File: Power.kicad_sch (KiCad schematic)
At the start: 34 parts, among them U1 LP87702DRHBRQ1

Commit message: finding exact crystal used in ref design, finishing shcematics
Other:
- note added: "Decoupling Caps"
- note added: "LC filtering"
- note added: "volt regulators, battery charger, and stepdowns"
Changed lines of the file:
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@@
+    (effects (font (size 1.27 1.27)) (justify left bottom))
+  )
+  (text "LC filtering\n" (at 243.84 66.04 0)
+    (effects (font (size 1.27 1.27)) (justify left bottom))
+  )
+  (text "volt regulators, battery charger, and stepdowns" (at 228.6 17.78 0)
+    (effects (font (size 1.27 1.27)) (justify left bottom))
+  )
+  (text "Decoupling Caps\n" (at 241.3 92.71 0)
     (effects (font (size 1.27 1.27)) (justify left bottom))
   )

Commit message: squashing ERC errors
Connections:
- net +3V3: no longer C1.2, C2.2, C3.1, C4.1, L1.2, R1.1, R2.1, R3.1, R4.1, U1.13 (VIN_B1), U1.14 (VIN_B1), U1.27 (VIN_B0), U1.28 (VIN_B0)
- net 1V24: no longer R8.2
- net 1V8: no longer R9.2
- net PMIC_EN1 renamed 3V3_REF
- net 3V3_REF: now also C1.2, C2.2, C3.1, C4.1, L1.2, R1.1, R2.1, R3.1, R4.1, U1.13 (VIN_B1), U1.14 (VIN_B1), U1.27 (VIN_B0), U1.28 (VIN_B0)
- new net AWR_1V24: R8.2
- new net AWR_1V8: R9.2
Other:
- note added: "voltage monitoring 1V24"
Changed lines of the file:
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@@
   (junction (at 60.96 166.37) (diameter 0) (color 0 0 0 0)
+  )
+  (junction (at 25.4 115.57) (diameter 0) (color 0 0 0 0)
   )
   (junction (at 146.05 162.56) (diameter 0) (color 0 0 0 0)
@@
     (stroke (width 0) (type default))
   )
-  (wire (pts (xy 45.72 113.03) (xy 41.91 113.03))
+  (wire (pts (xy 25.4 111.76) (xy 53.34 111.76))
     (stroke (width 0) (type default))
   )
@@
     (stroke (width 0) (type default))
   )
+  (wire (pts (xy 25.4 115.57) (xy 25.4 121.92))
+    (stroke (width 0) (type default))
+  )
   (wire (pts (xy 179.07 86.36) (xy 179.07 90.17))
     (stroke (width 0) (type default))
@@
     (stroke (width 0) (type default))
   )
-  (wire (pts (xy 52.07 104.14) (xy 52.07 110.49))
+  (wire (pts (xy 53.34 104.14) (xy 53.34 111.76))
     (stroke (width 0) (type default))
   )
@@
     (stroke (width 0) (type default))
   )
-  (wire (pts (xy 36.83 121.92) (xy 24.13 121.92))
+  (wire (pts (xy 36.83 121.92) (xy 25.4 121.92))
     (stroke (width 0) (type default))
   )
@@
     (stroke (width 0) (type default))
   )
-  (wire (pts (xy 52.07 110.49) (xy 45.72 110.49))
-    (stroke (width 0) (type default))
-  )
   (wire (pts (xy 148.59 101.6) (xy 154.94 101.6))
     (stroke (width 0) (type default))
@@
     (stroke (width 0) (type default))
   )
-  (wire (pts (xy 45.72 110.49) (xy 45.72 113.03))
-    (stroke (width 0) (type default))
-  )
   (wire (pts (xy 76.2 116.84) (xy 76.2 128.27))
     (stroke (width 0) (type default))
@@
     (stroke (width 0) (type default))
   )
+  (wire (pts (xy 25.4 111.76) (xy 25.4 115.57))
+    (stroke (width 0) (type default))
+  )
   (wire (pts (xy 34.29 73.66) (xy 40.64 73.66))
     (stroke (width 0) (type default))
@@
     (stroke (width 0) (type default))
   )
+  (wire (pts (xy 22.86 115.57) (xy 25.4 115.57))
+    (stroke (width 0) (type default))
+  )
   (wire (pts (xy 68.58 111.76) (xy 68.58 157.48))
     (stroke (width 0) (type default))
@@
     (stroke (width 0) (type default))
   )
-  (wire (pts (xy 50.8 158.75) (xy 50.8 161.29))
+  (wire (pts (xy 50.8 154.94) (xy 50.8 161.29))
     (stroke (width 0) (type default))
   )
@@
     (stroke (width 0) (type default))
   )
-  (wire (pts (xy 52.07 104.14) (xy 62.23 104.14))
+  (wire (pts (xy 53.34 104.14) (xy 62.23 104.14))
     (stroke (width 0) (type default))
   )
@@
     (effects (font (size 1.27 1.27)) (justify left bottom))
   )
+  (text "voltage monitoring 1V24\n" (at 119.38 135.89 0)
+    (effects (font (size 1.27 1.27)) (justify left bottom))
+  )
+  (text "voltage monitoring 1V24\n" (at 106.68 173.99 0)
+    (effects (font (size 1.27 1.27)) (justify left bottom))
+  )
   (text "Decoupling Caps\n" (at 241.3 92.71 0)
     (effects (font (size 1.27 1.27)) (justify left bottom))
-  )
-  (global_label "PMIC_EN1" (shape input) (at 41.91 113.03 180) (fields_autoplaced)
-    (effects (font (size 1.27 1.27)) (justify right))
-    (property "Intersheetrefs" "${INTERSHEET_REFS}" (at 29.672 113.03 0)
-      (effects (font (size 1.27 1.27)) (justify right) hide)
-    )
   )
   (global_label "AWR_PMIC_CLKOUT_SOP2" (shape input) (at 60.96 176.53 0) (fields_autoplaced)
@@
     )
   )
-  (global_label "1V24" (shape input) (at 101.6 168.91 0) (fields_autoplaced)
+  (global_label "AWR_1V24" (shape input) (at 101.6 168.91 0) (fields_autoplaced)
     (effects (font (size 1.27 1.27)) (justify left))
-    (property "Intersheetrefs" "${INTERSHEET_REFS}" (at 109.3023 168.91 0)
+    (property "Intersheetrefs" "${INTERSHEET_REFS}" (at 114.0799 168.91 0)
       (effects (font (size 1.27 1.27)) (justify left) hide)
     )
@@
     )
   )
-  (global_label "1V8" (shape input) (at 125.73 129.54 0) (fields_autoplaced)
+  (global_label "AWR_1V8" (shape input) (at 125.73 129.54 0) (fields_autoplaced)
     (effects (font (size 1.27 1.27)) (justify left))
-    (property "Intersheetrefs" "${INTERSHEET_REFS}" (at 132.2228 129.54 0)
+    (property "Intersheetrefs" "${INTERSHEET_REFS}" (at 137.0004 129.54 0)
       (effects (font (size 1.27 1.27)) (justify left) hide)
     )
@@
     )
   )
+  (global_label "3V3_REF" (shape output) (at 50.8 154.94 180) (fields_autoplaced)
+    (effects (font (size 1.27 1.27)) (justify right))
+    (property "Intersheetrefs" "${INTERSHEET_REFS}" (at 39.832 154.94 0)
+      (effects (font (size 1.27 1.27)) (justify right) hide)
+    )
+  )
   (global_label "AWR_MCUCLKOUT" (shape input) (at 93.98 128.27 0) (fields_autoplaced)
     (effects (font (size 1.27 1.27)) (justify left))
@@
     )
   )
+  (global_label "3V3_REF" (shape output) (at 22.86 115.57 180) (fields_autoplaced)
+    (effects (font (size 1.27 1.27)) (justify right))
+    (property "Intersheetrefs" "${INTERSHEET_REFS}" (at 11.892 115.57 0)
+      (effects (font (size 1.27 1.27)) (justify right) hide)
+    )
+  )
   (global_label "5VBST" (shape input) (at 171.45 82.55 180) (fields_autoplaced)
     (effects (font (size 1.27 1.27)) (justify right))
@@
     (effects (font (size 1.27 1.27)) (justify right))
     (property "Intersheetrefs" "${INTERSHEET_REFS}" (at 30.6396 106.68 0)
+      (effects (font (size 1.27 1.27)) (justify right) hide)
+    )
+  )
+  (global_label "3V3_REF" (shape output) (at 40.64 25.4 180) (fields_autoplaced)
+    (effects (font (size 1.27 1.27)) (justify right))
+    (property "Intersheetrefs" "${INTERSHEET_REFS}" (at 29.672 25.4 0)
       (effects (font (size 1.27 1.27)) (justify right) hide)
     )
@@
     )
   )
-  (symbol (lib_id "power:+3V3") (at 40.64 25.4 0) (unit 1)
-    (in_bom yes) (on_board yes) (dnp no)
-    (property "Reference" "#PWR014" (at 40.64 29.21 0)
-      (effects (font (size 1.27 1.27)) hide)
-    )
-    (property "Value" "+3V3" (at 40.64 21.59 0)
-      (effects (font (size 1.27 1.27)))
-    )
-    (property "Footprint" "" (at 40.64 25.4 0)
-      (effects (font (size 1.27 1.27)) hide)
-    )
-    (property "Datasheet" "" (at 40.64 25.4 0)
-      (effects (font (size 1.27 1.27)) hide)
-    )
-    (pin "1")
-    (instances
-      (project "radar"
-        (path "/88b309aa-5f0e-45d7-beec-81d4b0ee2121/7a3c78f1-80f2-463b-a37f-9a7b3cc7f964"
-          (reference "#PWR014") (unit 1)
-        )
-      )
-    )
-  )
   (symbol (lib_id "power:GND") (at 171.45 123.19 0) (unit 1)
     (in_bom yes) (on_board yes) (dnp no) (fields_autoplaced)
@@
     )
   )
-  (symbol (lib_id "power:+3V3") (at 24.13 121.92 0) (unit 1)
-    (in_bom yes) (on_board yes) (dnp no)
-    (property "Reference" "#PWR018" (at 24.13 125.73 0)
-      (effects (font (size 1.27 1.27)) hide)
-    )
-    (property "Value" "+3V3" (at 24.13 116.84 0)
-      (effects (font (size 1.27 1.27)))
-    )
-    (property "Footprint" "" (at 24.13 121.92 0)
-      (effects (font (size 1.27 1.27)) hide)
-    )
-    (property "Datasheet" "" (at 24.13 121.92 0)
-      (effects (font (size 1.27 1.27)) hide)
-    )
-    (pin "1")
-    (instances
-      (project "radar"
-        (path "/88b309aa-5f0e-45d7-beec-81d4b0ee2121/7a3c78f1-80f2-463b-a37f-9a7b3cc7f964"
-          (reference "#PWR018") (unit 1)
-        )
-      )
-    )
-  )
   (symbol (lib_id "Device:R_Small_US") (at 148.59 63.5 90) (unit 1)
     (in_bom yes) (on_board yes) (dnp no)
@@
         )
       )
-    )
-  )
-  (symbol (lib_id "power:+3V3") (at 50.8 158.75 0) (unit 1)
-    (in_bom yes) (on_board yes) (dnp no) (fields_autoplaced)
-    (property "Reference" "#PWR019" (at 50.8 162.56 0)
-      (effects (font (size 1.27 1.27)) hide)
-    )
-    (property "Value" "+3V3" (at 50.8 153.67 0)
-      (effects (font (size 1.27 1.27)))
-    )
-    (property "Footprint" "" (at 50.8 158.75 0)
-      (effects (font (size 1.27 1.27)) hide)
-    )
-    (property "Datasheet" "" (at 50.8 158.75 0)
-      (effects (font (size 1.27 1.27)) hide)
-    )
-    (pin "1")
-    (instances
-      (project "radar"
-        (path "/88b309aa-5f0e-45d7-beec-81d4b0ee2121/7a3c78f1-80f2-463b-a37f-9a7b3cc7f964"
-          (reference "#PWR019") (unit 1)
-        )
-      )

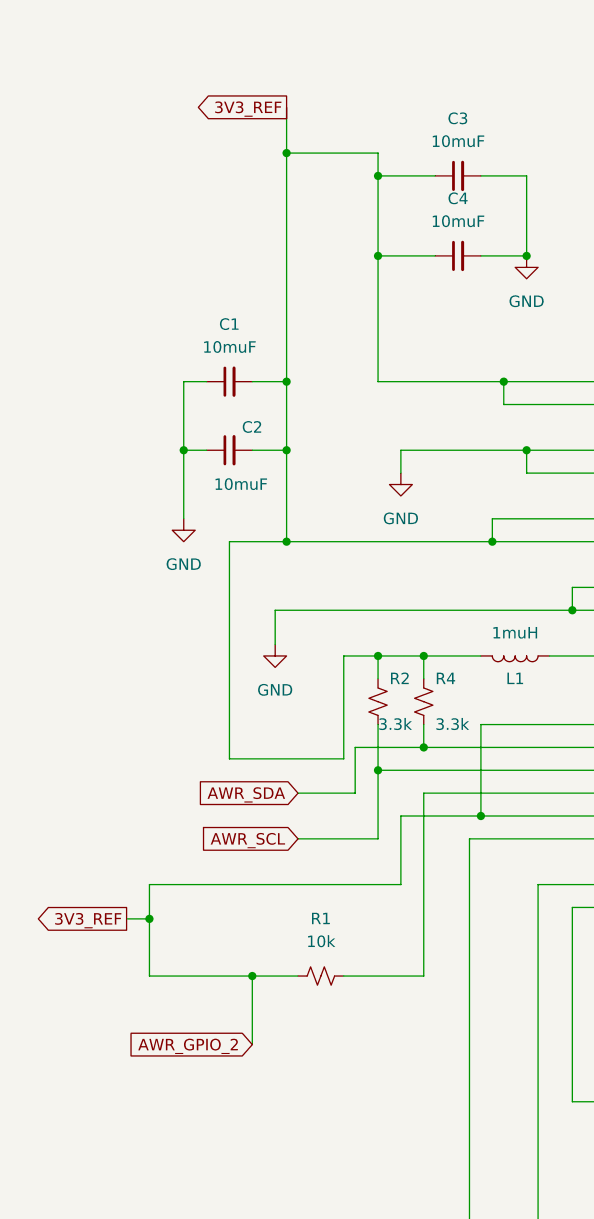
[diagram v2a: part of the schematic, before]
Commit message: squashed ERC errors, moving onto pcb, grabbing fuse footprint
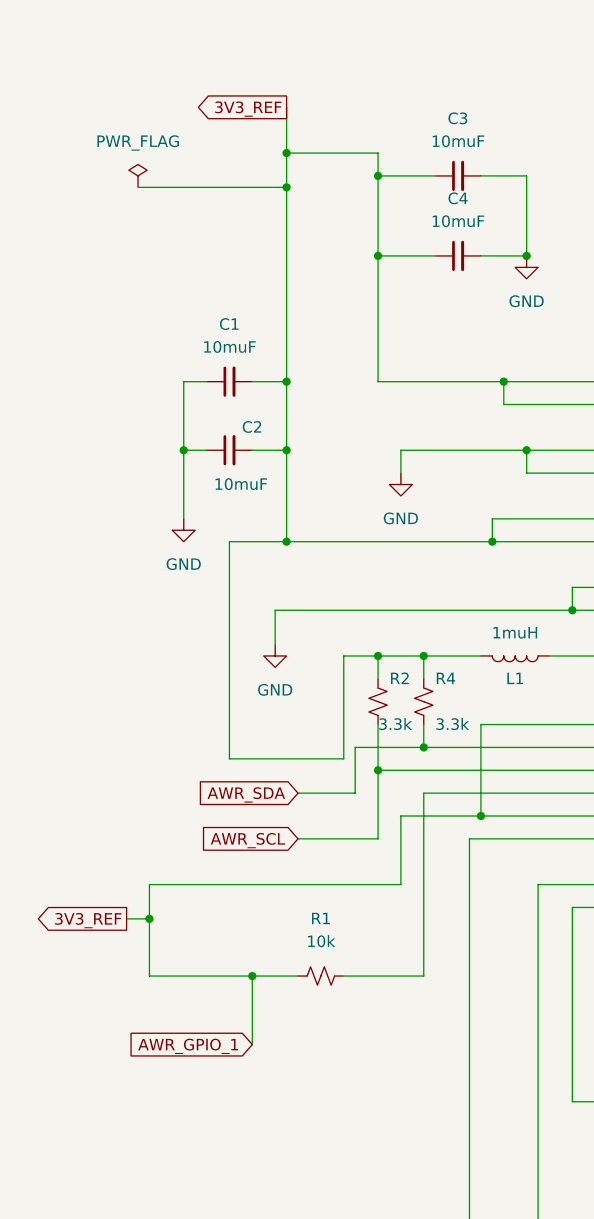
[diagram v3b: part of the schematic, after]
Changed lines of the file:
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@@
   (junction (at 173.99 97.79) (diameter 0) (color 0 0 0 0)
+  )
+  (junction (at 40.64 34.29) (diameter 0) (color 0 0 0 0)
   )
   (junction (at 171.45 116.84) (diameter 0) (color 0 0 0 0)
@@
     (stroke (width 0) (type default))
   )
+  (wire (pts (xy 40.64 34.29) (xy 40.64 55.88))
+    (stroke (width 0) (type default))
+  )
   (wire (pts (xy 151.13 170.18) (xy 157.48 170.18))
     (stroke (width 0) (type default))
@@
     (stroke (width 0) (type default))
   )
-  (wire (pts (xy 40.64 30.48) (xy 40.64 55.88))
+  (wire (pts (xy 40.64 30.48) (xy 40.64 34.29))
     (stroke (width 0) (type default))
   )
@@
   )
   (wire (pts (xy 173.99 97.79) (xy 165.1 97.79))
+    (stroke (width 0) (type default))
+  )
+  (wire (pts (xy 24.13 34.29) (xy 40.64 34.29))
     (stroke (width 0) (type default))
   )
@@
     )
   )
-  (global_label "AWR_GPIO_2" (shape input) (at 36.83 129.54 180) (fields_autoplaced)
+  (global_label "AWR_GPIO_1" (shape input) (at 36.83 129.54 180) (fields_autoplaced)
     (effects (font (size 1.27 1.27)) (justify right))
     (property "Intersheetrefs" "${INTERSHEET_REFS}" (at 22.4148 129.54 0)
@@
         )
       )
+    )
+  )
+  (symbol (lib_id "power:PWR_FLAG") (at 24.13 34.29 0) (unit 1)
+    (in_bom yes) (on_board yes) (dnp no) (fields_autoplaced)
+    (property "Reference" "#FLG06" (at 24.13 32.385 0)
+      (effects (font (size 1.27 1.27)) hide)
+    )
+    (property "Value" "PWR_FLAG" (at 24.13 29.21 0)
+      (effects (font (size 1.27 1.27)))
+    )
+    (property "Footprint" "" (at 24.13 34.29 0)
+      (effects (font (size 1.27 1.27)) hide)
+    )
+    (property "Datasheet" "~" (at 24.13 34.29 0)
+      (effects (font (size 1.27 1.27)) hide)
+    )
+    (pin "1")
+    (instances
+      (project "radar"
+        (path "/88b309aa-5f0e-45d7-beec-81d4b0ee2121/7a3c78f1-80f2-463b-a37f-9a7b3cc7f964"
+          (reference "#FLG06") (unit 1)
+        )
+      )

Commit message: adding footprints
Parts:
- C1, C2, C21, C22, C23, C24, C25, C26, C27, C28, C29, C3, C30, C31, C4: footprint (none) -> Capacitor_SMD:C_0603_1608Metric
- L1, L2, L3: footprint (none) -> Inductor_SMD:L_0603_1608Metric
- R1, R12, R13, R14, R15, R2, R26, R27, R3, R4, R5, R6, R7, R8, R9: footprint (none) -> Resistor_SMD:R_0603_1608Metric
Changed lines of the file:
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@@
       (effects (font (size 1.27 1.27)) (justify left))
     )
-    (property "Footprint" "" (at 189.23 77.47 0)
+    (property "Footprint" "Capacitor_SMD:C_0603_1608Metric" (at 189.23 77.47 0)
       (effects (font (size 1.27 1.27)) hide)
     )
@@
       (effects (font (size 1.27 1.27)) (justify left))
     )
-    (property "Footprint" "" (at 50.8 163.83 0)
+    (property "Footprint" "Resistor_SMD:R_0603_1608Metric" (at 50.8 163.83 0)
       (effects (font (size 1.27 1.27)) hide)
     )
@@
       (effects (font (size 1.27 1.27)))
     )
-    (property "Footprint" "" (at 170.18 137.16 0)
+    (property "Footprint" "Resistor_SMD:R_0603_1608Metric" (at 170.18 137.16 0)
       (effects (font (size 1.27 1.27)) hide)
     )
@@
       (effects (font (size 1.27 1.27)) (justify left))
     )
-    (property "Footprint" "" (at 165.1 91.44 0)
+    (property "Footprint" "Capacitor_SMD:C_0603_1608Metric" (at 165.1 91.44 0)
       (effects (font (size 1.27 1.27)) hide)
     )
@@
       (effects (font (size 1.27 1.27)))
     )
-    (property "Footprint" "" (at 146.05 78.74 0)
+    (property "Footprint" "Resistor_SMD:R_0603_1608Metric" (at 146.05 78.74 0)
       (effects (font (size 1.27 1.27)) hide)
     )
@@
       (effects (font (size 1.27 1.27)) (justify left))
     )
-    (property "Footprint" "" (at 170.18 59.69 0)
+    (property "Footprint" "Capacitor_SMD:C_0603_1608Metric" (at 170.18 59.69 0)
       (effects (font (size 1.27 1.27)) hide)
     )
@@
       (effects (font (size 1.27 1.27)) (justify left))
     )
-    (property "Footprint" "" (at 92.71 162.56 0)
+    (property "Footprint" "Resistor_SMD:R_0603_1608Metric" (at 92.71 162.56 0)
       (effects (font (size 1.27 1.27)) hide)
     )
@@
       (effects (font (size 1.27 1.27)) (justify left))
     )
-    (property "Footprint" "" (at 55.88 91.44 0)
+    (property "Footprint" "Resistor_SMD:R_0603_1608Metric" (at 55.88 91.44 0)
       (effects (font (size 1.27 1.27)) hide)
     )
@@
       (effects (font (size 1.27 1.27)))
     )
-    (property "Footprint" "" (at 44.45 121.92 0)
+    (property "Footprint" "Resistor_SMD:R_0603_1608Metric" (at 44.45 121.92 0)
       (effects (font (size 1.27 1.27)) hide)
     )
@@
       (effects (font (size 1.27 1.27)))
     )
-    (property "Footprint" "" (at 138.43 158.75 0)
+    (property "Footprint" "Capacitor_SMD:C_0603_1608Metric" (at 138.43 158.75 0)
       (effects (font (size 1.27 1.27)) hide)
     )
@@
       (effects (font (size 1.27 1.27)))
     )
-    (property "Footprint" "" (at 59.69 41.91 0)
+    (property "Footprint" "Capacitor_SMD:C_0603_1608Metric" (at 59.69 41.91 0)
       (effects (font (size 1.27 1.27)) hide)
     )
@@
       (effects (font (size 1.27 1.27)))
     )
-    (property "Footprint" "" (at 119.38 129.54 0)
+    (property "Footprint" "Resistor_SMD:R_0603_1608Metric" (at 119.38 129.54 0)
       (effects (font (size 1.27 1.27)) hide)
     )
@@
       (effects (font (size 1.27 1.27)) (justify left))
     )
-    (property "Footprint" "" (at 171.45 119.38 0)
+    (property "Footprint" "Capacitor_SMD:C_0603_1608Metric" (at 171.45 119.38 0)
       (effects (font (size 1.27 1.27)) hide)
     )
@@
       (effects (font (size 1.27 1.27)) (justify left))
     )
-    (property "Footprint" "" (at 50.8 91.44 0)
+    (property "Footprint" "Resistor_SMD:R_0603_1608Metric" (at 50.8 91.44 0)
       (effects (font (size 1.27 1.27)) hide)
     )
@@
       (effects (font (size 1.27 1.27)) (justify left))
     )
-    (property "Footprint" "" (at 146.05 165.1 0)
+    (property "Footprint" "Capacitor_SMD:C_0603_1608Metric" (at 146.05 165.1 0)
       (effects (font (size 1.27 1.27)) hide)
     )
@@
       (effects (font (size 1.27 1.27)))
     )
-    (property "Footprint" "" (at 34.29 55.88 0)
+    (property "Footprint" "Capacitor_SMD:C_0603_1608Metric" (at 34.29 55.88 0)
       (effects (font (size 1.27 1.27)) hide)
     )
@@
       (effects (font (size 1.27 1.27)))
     )
-    (property "Footprint" "" (at 34.29 63.5 0)
+    (property "Footprint" "Capacitor_SMD:C_0603_1608Metric" (at 34.29 63.5 0)
       (effects (font (size 1.27 1.27)) hide)
     )
@@
       (effects (font (size 1.27 1.27)))
     )
-    (property "Footprint" "" (at 151.13 73.66 0)
+    (property "Footprint" "Inductor_SMD:L_0603_1608Metric" (at 151.13 73.66 0)
       (effects (font (size 1.27 1.27)) hide)
     )
@@
       (effects (font (size 1.27 1.27)))
     )
-    (property "Footprint" "" (at 59.69 33.02 0)
+    (property "Footprint" "Capacitor_SMD:C_0603_1608Metric" (at 59.69 33.02 0)
       (effects (font (size 1.27 1.27)) hide)
     )
@@
       (effects (font (size 1.27 1.27)) (justify left))
     )
-    (property "Footprint" "" (at 179.07 92.71 0)
+    (property "Footprint" "Capacitor_SMD:C_0603_1608Metric" (at 179.07 92.71 0)
       (effects (font (size 1.27 1.27)) hide)
     )
@@
       (effects (font (size 1.27 1.27)))
     )
-    (property "Footprint" "" (at 148.59 63.5 0)
+    (property "Footprint" "Resistor_SMD:R_0603_1608Metric" (at 148.59 63.5 0)
       (effects (font (size 1.27 1.27)) hide)
     )
@@
       (effects (font (size 1.27 1.27)))
     )
-    (property "Footprint" "" (at 66.04 86.36 0)
+    (property "Footprint" "Inductor_SMD:L_0603_1608Metric" (at 66.04 86.36 0)
       (effects (font (size 1.27 1.27)) hide)
     )
@@
       (effects (font (size 1.27 1.27)) (justify left))
     )
-    (property "Footprint" "" (at 101.6 162.56 0)
+    (property "Footprint" "Resistor_SMD:R_0603_1608Metric" (at 101.6 162.56 0)
       (effects (font (size 1.27 1.27)) hide)
     )
@@
       (effects (font (size 1.27 1.27)) (justify left))
     )
-    (property "Footprint" "" (at 182.88 110.49 0)
+    (property "Footprint" "Resistor_SMD:R_0603_1608Metric" (at 182.88 110.49 0)
       (effects (font (size 1.27 1.27)) hide)
     )
@@
       (effects (font (size 1.27 1.27)))
     )
-    (property "Footprint" "" (at 149.86 55.88 0)
+    (property "Footprint" "Inductor_SMD:L_0603_1608Metric" (at 149.86 55.88 0)
       (effects (font (size 1.27 1.27)) hide)
     )
@@
       (effects (font (size 1.27 1.27)) (justify left))
     )
-    (property "Footprint" "" (at 176.53 77.47 0)
+    (property "Footprint" "Capacitor_SMD:C_0603_1608Metric" (at 176.53 77.47 0)
       (effects (font (size 1.27 1.27)) hide)
     )
@@
       (effects (font (size 1.27 1.27)) (justify left))
     )
-    (property "Footprint" "" (at 76.2 162.56 0)
+    (property "Footprint" "Capacitor_SMD:C_0603_1608Metric" (at 76.2 162.56 0)
       (effects (font (size 1.27 1.27)) hide)
     )
@@
       (effects (font (size 1.27 1.27)))
     )
-    (property "Footprint" "" (at 85.09 128.27 0)
+    (property "Footprint" "Resistor_SMD:R_0603_1608Metric" (at 85.09 128.27 0)
       (effects (font (size 1.27 1.27)) hide)
     )
@@
       (effects (font (size 1.27 1.27)))
     )
-    (property "Footprint" "" (at 144.78 104.14 0)
+    (property "Footprint" "Resistor_SMD:R_0603_1608Metric" (at 144.78 104.14 0)
       (effects (font (size 1.27 1.27)) hide)
     )
@@
       (effects (font (size 1.27 1.27)))
     )
-    (property "Footprint" "" (at 144.78 99.06 0)
+    (property "Footprint" "Resistor_SMD:R_0603_1608Metric" (at 144.78 99.06 0)
       (effects (font (size 1.27 1.27)) hide)
     )
@@
       (effects (font (size 1.27 1.27)) (justify left))
     )
-    (property "Footprint" "" (at 116.84 140.97 0)
+    (property "Footprint" "Capacitor_SMD:C_0603_1608Metric" (at 116.84 140.97 0)
       (effects (font (size 1.27 1.27)) hide)
     )
@@
       (effects (font (size 1.27 1.27)) (justify left))
     )
-    (property "Footprint" "" (at 157.48 165.1 0)
+    (property "Footprint" "Capacitor_SMD:C_0603_1608Metric" (at 157.48 165.1 0)
       (effects (font (size 1.27 1.27)) hide)
     )
@@
       (effects (font (size 1.27 1.27)))
     )
-    (property "Footprint" "" (at 55.88 166.37 0)
-      (effects (font (size 1.27 1.27)) hide)
-    )
+    (property "Footprint" "Resistor_SMD:R_0603_1608Metric" (at 55.88 166.37 0)
+      (effects (font (size 1.27 1.27)) hide)
+    )
